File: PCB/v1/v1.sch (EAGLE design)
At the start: 72 parts, among them U2 AT24C512C-SHD-B

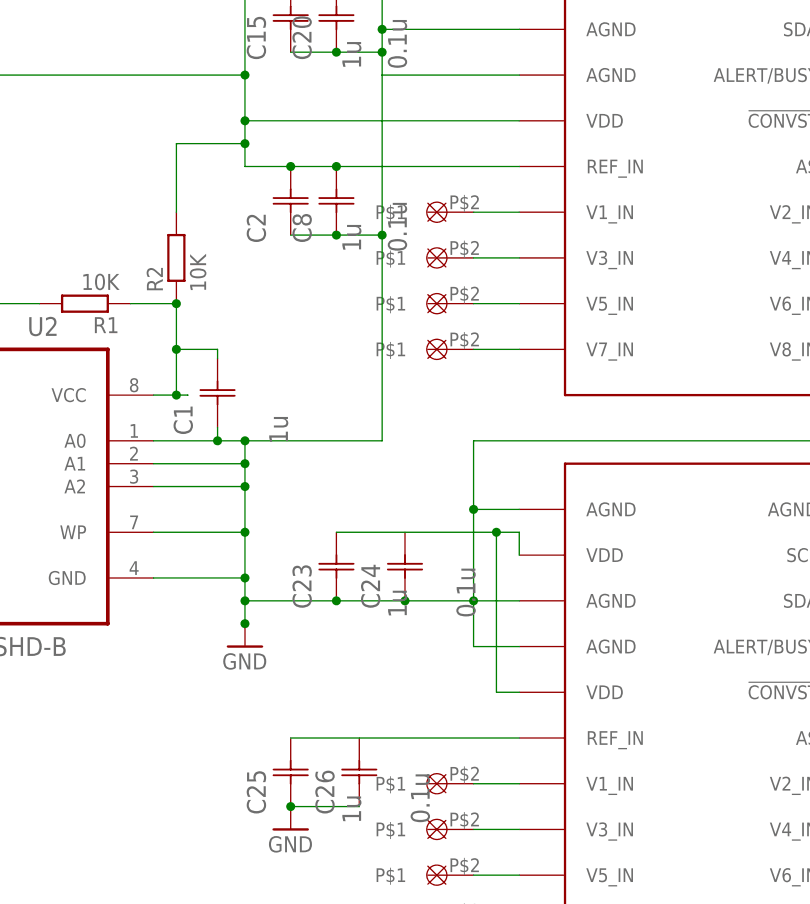
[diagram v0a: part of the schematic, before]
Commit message: need to remove drill holes and go through checklist
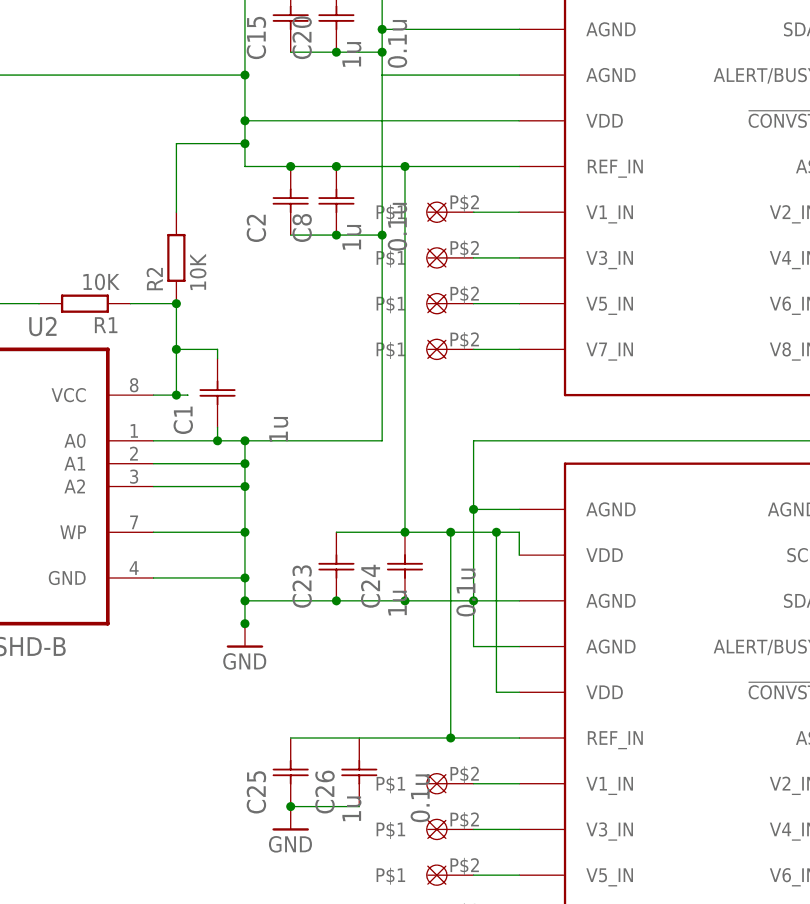
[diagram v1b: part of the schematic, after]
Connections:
- removed net N$10: C25.C2, U$6.REF_IN
- removed net N$8: C23.C2, U$6.VDD@1, U$6.VDD@2
- net VDD: now also C23.C2, C24.C2, C25.C2, U$6.REF_IN, U$6.VDD@1, U$6.VDD@2
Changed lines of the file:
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@@
 <wire x1="76.2" y1="88.9" x2="86.36" y2="88.9" width="0.1524" layer="91"/>
 <junction x="76.2" y="88.9"/>
-<wire x1="86.36" y1="88.9" x2="93.98" y2="88.9" width="0.1524" layer="91"/>
-<wire x1="93.98" y1="88.9" x2="101.6" y2="88.9" width="0.1524" layer="91"/>
 <wire x1="101.6" y1="99.06" x2="101.6" y2="106.68" width="0.1524" layer="91"/>
 <junction x="101.6" y="99.06"/>
@@
 <junction x="152.4" y="106.68"/>
 <pinref part="C23" gate="A" pin="C1"/>
+<pinref part="C24" gate="A" pin="C1"/>
+<wire x1="86.36" y1="88.9" x2="93.98" y2="88.9" width="0.1524" layer="91"/>
 <junction x="86.36" y="88.9"/>
-<pinref part="C24" gate="A" pin="C1"/>
+<wire x1="93.98" y1="88.9" x2="101.6" y2="88.9" width="0.1524" layer="91"/>
 <junction x="93.98" y="88.9"/>
 </segment>
@@
 <wire x1="76.2" y1="157.48" x2="76.2" y2="147.32" width="0.1524" layer="91"/>
 <wire x1="76.2" y1="147.32" x2="76.2" y2="142.24" width="0.1524" layer="91"/>
-<wire x1="106.68" y1="137.16" x2="86.36" y2="137.16" width="0.1524" layer="91"/>
+<wire x1="106.68" y1="137.16" x2="93.98" y2="137.16" width="0.1524" layer="91"/>
 <pinref part="C2" gate="A" pin="C2"/>
+<wire x1="93.98" y1="137.16" x2="86.36" y2="137.16" width="0.1524" layer="91"/>
 <wire x1="86.36" y1="137.16" x2="81.28" y2="137.16" width="0.1524" layer="91"/>
 <wire x1="81.28" y1="137.16" x2="76.2" y2="137.16" width="0.1524" layer="91"/>
@@
 <pinref part="VDD1" gate="G$1" pin="VDD"/>
 <junction x="76.2" y="157.48"/>
+<wire x1="93.98" y1="137.16" x2="93.98" y2="96.52" width="0.1524" layer="91"/>
+<junction x="93.98" y="137.16"/>
+<pinref part="C24" gate="A" pin="C2"/>
+<pinref part="C23" gate="A" pin="C2"/>
+<wire x1="86.36" y1="96.52" x2="93.98" y2="96.52" width="0.1524" layer="91"/>
+<junction x="93.98" y="96.52"/>
+<pinref part="C25" gate="A" pin="C2"/>
+<pinref part="U$6" gate="G$1" pin="REF_IN"/>
+<wire x1="106.68" y1="73.66" x2="99.06" y2="73.66" width="0.1524" layer="91"/>
+<pinref part="U$6" gate="G$1" pin="VDD@1"/>
+<wire x1="106.68" y1="93.98" x2="106.68" y2="96.52" width="0.1524" layer="91"/>
+<wire x1="106.68" y1="96.52" x2="104.14" y2="96.52" width="0.1524" layer="91"/>
+<pinref part="U$6" gate="G$1" pin="VDD@2"/>
+<wire x1="106.68" y1="78.74" x2="104.14" y2="78.74" width="0.1524" layer="91"/>
+<wire x1="104.14" y1="78.74" x2="104.14" y2="96.52" width="0.1524" layer="91"/>
+<junction x="104.14" y="96.52"/>
+<wire x1="104.14" y1="96.52" x2="99.06" y2="96.52" width="0.1524" layer="91"/>
+<wire x1="99.06" y1="96.52" x2="99.06" y2="73.66" width="0.1524" layer="91"/>
+<junction x="99.06" y="73.66"/>
+<wire x1="99.06" y1="73.66" x2="81.28" y2="73.66" width="0.1524" layer="91"/>
+<wire x1="99.06" y1="96.52" x2="93.98" y2="96.52" width="0.1524" layer="91"/>
+<junction x="99.06" y="96.52"/>
 </segment>
 <segment>
@@
 </segment>
 </net>
-<net name="N$8" class="0">
-<segment>
-<pinref part="U$6" gate="G$1" pin="VDD@1"/>
-<wire x1="106.68" y1="93.98" x2="106.68" y2="96.52" width="0.1524" layer="91"/>
-<pinref part="C23" gate="A" pin="C2"/>
-<wire x1="106.68" y1="96.52" x2="104.14" y2="96.52" width="0.1524" layer="91"/>
-<pinref part="U$6" gate="G$1" pin="VDD@2"/>
-<wire x1="104.14" y1="96.52" x2="86.36" y2="96.52" width="0.1524" layer="91"/>
-<wire x1="106.68" y1="78.74" x2="104.14" y2="78.74" width="0.1524" layer="91"/>
-<wire x1="104.14" y1="78.74" x2="104.14" y2="96.52" width="0.1524" layer="91"/>
-<junction x="104.14" y="96.52"/>
-</segment>
-</net>
-<net name="N$10" class="0">
-<segment>
-<pinref part="U$6" gate="G$1" pin="REF_IN"/>
-<pinref part="C25" gate="A" pin="C2"/>
-<wire x1="106.68" y1="73.66" x2="81.28" y2="73.66" width="0.1524" layer="91"/>
-</segment>
-</net>

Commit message: final checked + silk screen
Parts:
- removed R10, R11, R12, R13: 10K, rcl:R-EU_R0402
- added U$31: TEST_POINT_0.5MM, TEST_POINT_0.5mm:TEST_POINT_0.5MM
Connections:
- removed net N$108: R10.2
- removed net N$110: R11.2
- removed net N$113: R13.2
- net N$49: now also U$31.P$1
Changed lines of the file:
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@@
 <part name="C26" library="AVX_By_element14_Batch_1" deviceset="UQCL2A100JAT2A/500" device="" value="0.1u"/>
 <part name="GND14" library="supply1" deviceset="GND" device=""/>
-<part name="R10" library="rcl" deviceset="R-EU_" device="R0402" value="10K"/>
-<part name="R11" library="rcl" deviceset="R-EU_" device="R0402" value="10K"/>
-<part name="R12" library="rcl" deviceset="R-EU_" device="R0402" value="10K"/>
-<part name="R13" library="rcl" deviceset="R-EU_" device="R0402" value="10K"/>
-<part name="VDD4" library="supply1" deviceset="VDD" device=""/>
-<part name="VDD5" library="supply1" deviceset="VDD" device=""/>
 <part name="U$7" library="BATTERY_2996_2" deviceset="BATTERY_2996" device=""/>
 <part name="U$8" library="BATTERY_2996_2" deviceset="BATTERY_2996" device=""/>
@@
 <part name="U$30" library="TEST_POINT_0.5mm" deviceset="TEST_POINT_0.5MM" device=""/>
 <part name="U$2" library="MINI_SMT_8_PIN_CONNECTOR" deviceset="8PIN_SMT_CONNECTOR" device=""/>
+<part name="U$31" library="TEST_POINT_0.5mm" deviceset="TEST_POINT_0.5MM" device=""/>
 </parts>
 <sheets>
@@
 <instance part="C26" gate="A" x="88.9" y="66.04" rot="R90"/>
 <instance part="GND14" gate="1" x="81.28" y="63.5"/>
-<instance part="R10" gate="G$1" x="170.18" y="165.1" rot="R270"/>
-<instance part="R11" gate="G$1" x="177.8" y="165.1" rot="R270"/>
-<instance part="R12" gate="G$1" x="170.18" y="99.06" rot="R270"/>
-<instance part="R13" gate="G$1" x="177.8" y="99.06" rot="R270"/>
-<instance part="VDD4" gate="G$1" x="172.72" y="175.26"/>
-<instance part="VDD5" gate="G$1" x="172.72" y="109.22"/>
 <instance part="U$7" gate="G$1" x="-193.04" y="116.84"/>
 <instance part="U$8" gate="G$1" x="-193.04" y="142.24"/>
@@
 <instance part="U$30" gate="G$1" x="-55.88" y="12.7" rot="R180"/>
 <instance part="U$2" gate="G$1" x="43.18" y="-48.26"/>
+<instance part="U$31" gate="G$1" x="-109.22" y="58.42" rot="R90"/>
 </instances>
 <busses>
@@
 <junction x="99.06" y="96.52"/>
 </segment>
-<segment>
-<pinref part="VDD5" gate="G$1" pin="VDD"/>
-<wire x1="172.72" y1="106.68" x2="172.72" y2="104.14" width="0.1524" layer="91"/>
-</segment>
-<segment>
-<pinref part="VDD4" gate="G$1" pin="VDD"/>
-<wire x1="172.72" y1="172.72" x2="172.72" y2="170.18" width="0.1524" layer="91"/>
-</segment>
 </net>
 <net name="N$32" class="0">
@@
 <pinref part="U$1" gate="G$1" pin="WAKE"/>
 <pinref part="R7" gate="G$1" pin="1"/>
+<pinref part="U$31" gate="G$1" pin="P$1"/>
+<wire x1="-101.6" y1="58.42" x2="-104.14" y2="58.42" width="0.1524" layer="91"/>
+<junction x="-101.6" y="58.42"/>
 </segment>
 </net>
@@
 </segment>
 </net>
-<net name="N$108" class="0">
-<segment>
-<pinref part="R10" gate="G$1" pin="2"/>
-<wire x1="170.18" y1="157.48" x2="170.18" y2="160.02" width="0.1524" layer="91"/>
-</segment>
-</net>
-<net name="N$110" class="0">
-<segment>
-<pinref part="R11" gate="G$1" pin="2"/>
-<wire x1="177.8" y1="152.4" x2="177.8" y2="160.02" width="0.1524" layer="91"/>
-</segment>
-</net>
-<net name="N$113" class="0">
-<segment>
-<pinref part="R13" gate="G$1" pin="2"/>
-<wire x1="177.8" y1="88.9" x2="177.8" y2="93.98" width="0.1524" layer="91"/>
-</segment>
-</net>

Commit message: submitting for fabrication
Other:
- moved on the sheet: C5
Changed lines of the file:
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@@
 <instance part="C3" gate="A" x="-91.44" y="0" rot="R90"/>
 <instance part="C4" gate="A" x="-76.2" y="0" rot="R90"/>
-<instance part="C5" gate="A" x="-120.65" y="73.66" rot="R180"/>
+<instance part="C5" gate="A" x="-123.19" y="73.66" rot="R180"/>
 <instance part="C6" gate="A" x="-120.65" y="66.04" rot="R180"/>
 <instance part="GND3" gate="1" x="-83.82" y="-7.366"/>
@@
 <pinref part="C6" gate="A" pin="C2"/>
 <wire x1="-128.27" y1="66.04" x2="-129.54" y2="66.04" width="0.1524" layer="91"/>
-<wire x1="-129.54" y1="66.04" x2="-129.54" y2="73.66" width="0.1524" layer="91"/>
+<wire x1="-129.54" y1="66.04" x2="-129.54" y2="71.12" width="0.1524" layer="91"/>
 <junction x="-129.54" y="66.04"/>
-<wire x1="-127" y1="73.66" x2="-129.54" y2="73.66" width="0.1524" layer="91"/>
+<wire x1="-129.54" y1="71.12" x2="-132.08" y2="71.12" width="0.1524" layer="91"/>
+<wire x1="-132.08" y1="71.12" x2="-132.08" y2="73.66" width="0.1524" layer="91"/>
+<wire x1="-132.08" y1="73.66" x2="-129.54" y2="73.66" width="0.1524" layer="91"/>
 </segment>
 <segment>
@@
 <segment>
 <pinref part="C5" gate="A" pin="C1"/>
-<wire x1="-120.65" y1="73.66" x2="-115.57" y2="73.66" width="0.1524" layer="91"/>
+<wire x1="-123.19" y1="73.66" x2="-115.57" y2="73.66" width="0.1524" layer="91"/>
 <pinref part="U$4" gate="G$1" pin="P$2"/>
 <wire x1="-115.57" y1="73.66" x2="-96.52" y2="73.66" width="0.1524" layer="91"/>
